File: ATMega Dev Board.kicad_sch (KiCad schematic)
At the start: 44 parts, among them J1 Conn_01x09, J2 Conn_01x04, J3 Conn_01x09, J4 SPI header, J5 USB-C_31-M-12, Q1 S8050, Q2 2N7002, Q3 HL6042, Q4 HL6042, SW1 SW_SPST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

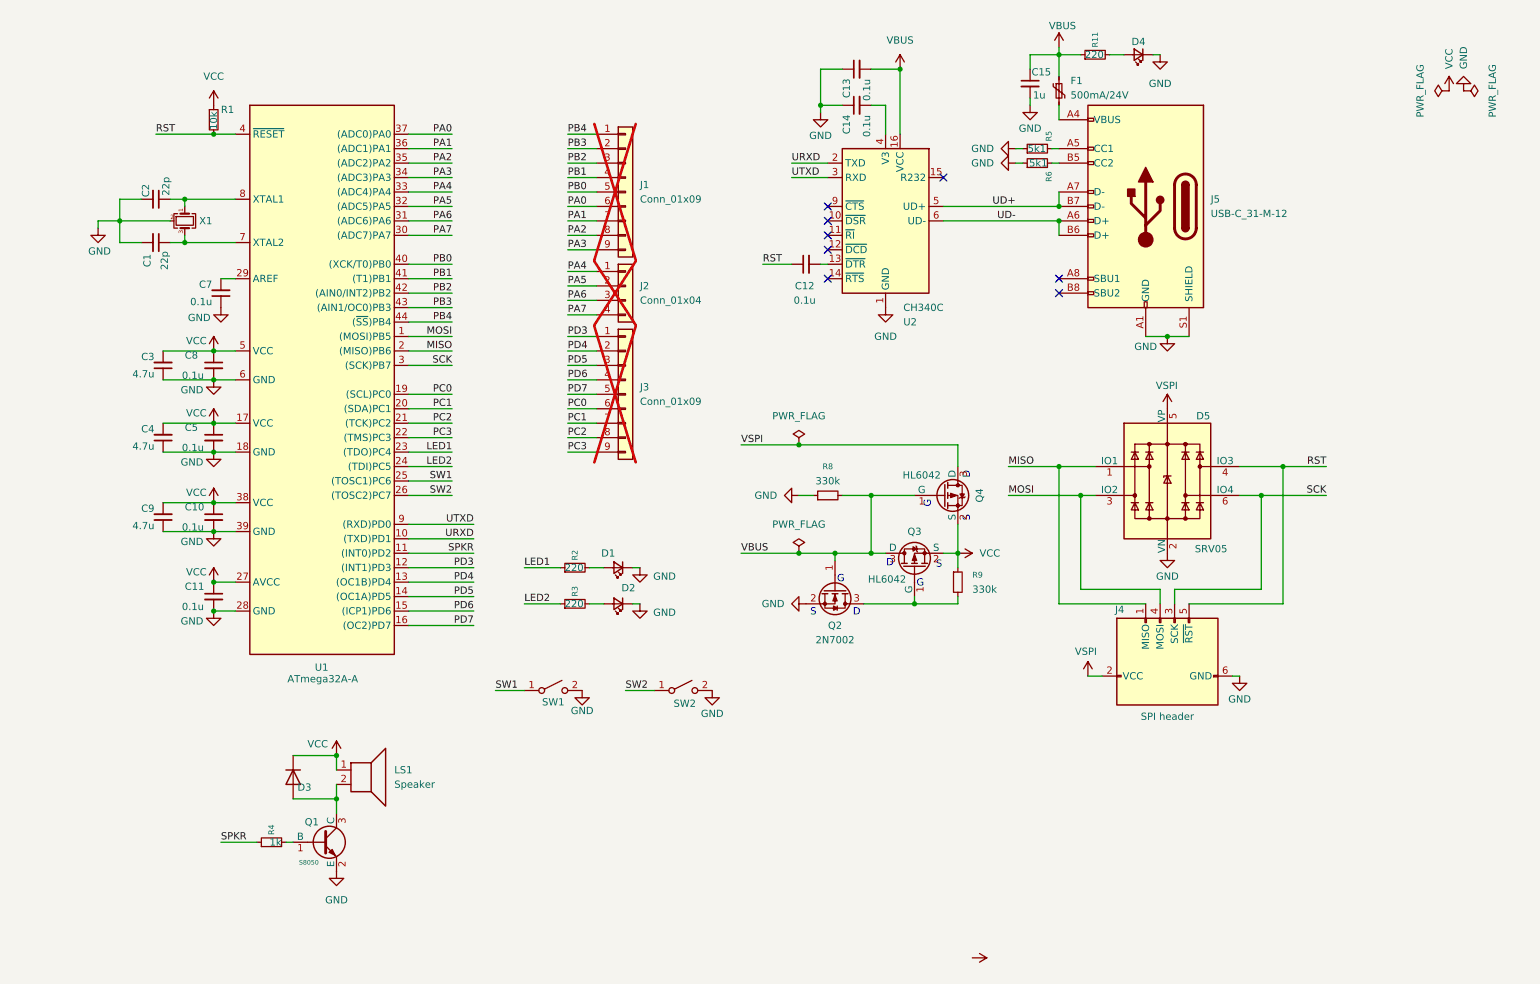
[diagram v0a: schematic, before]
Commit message: corrected usb connections
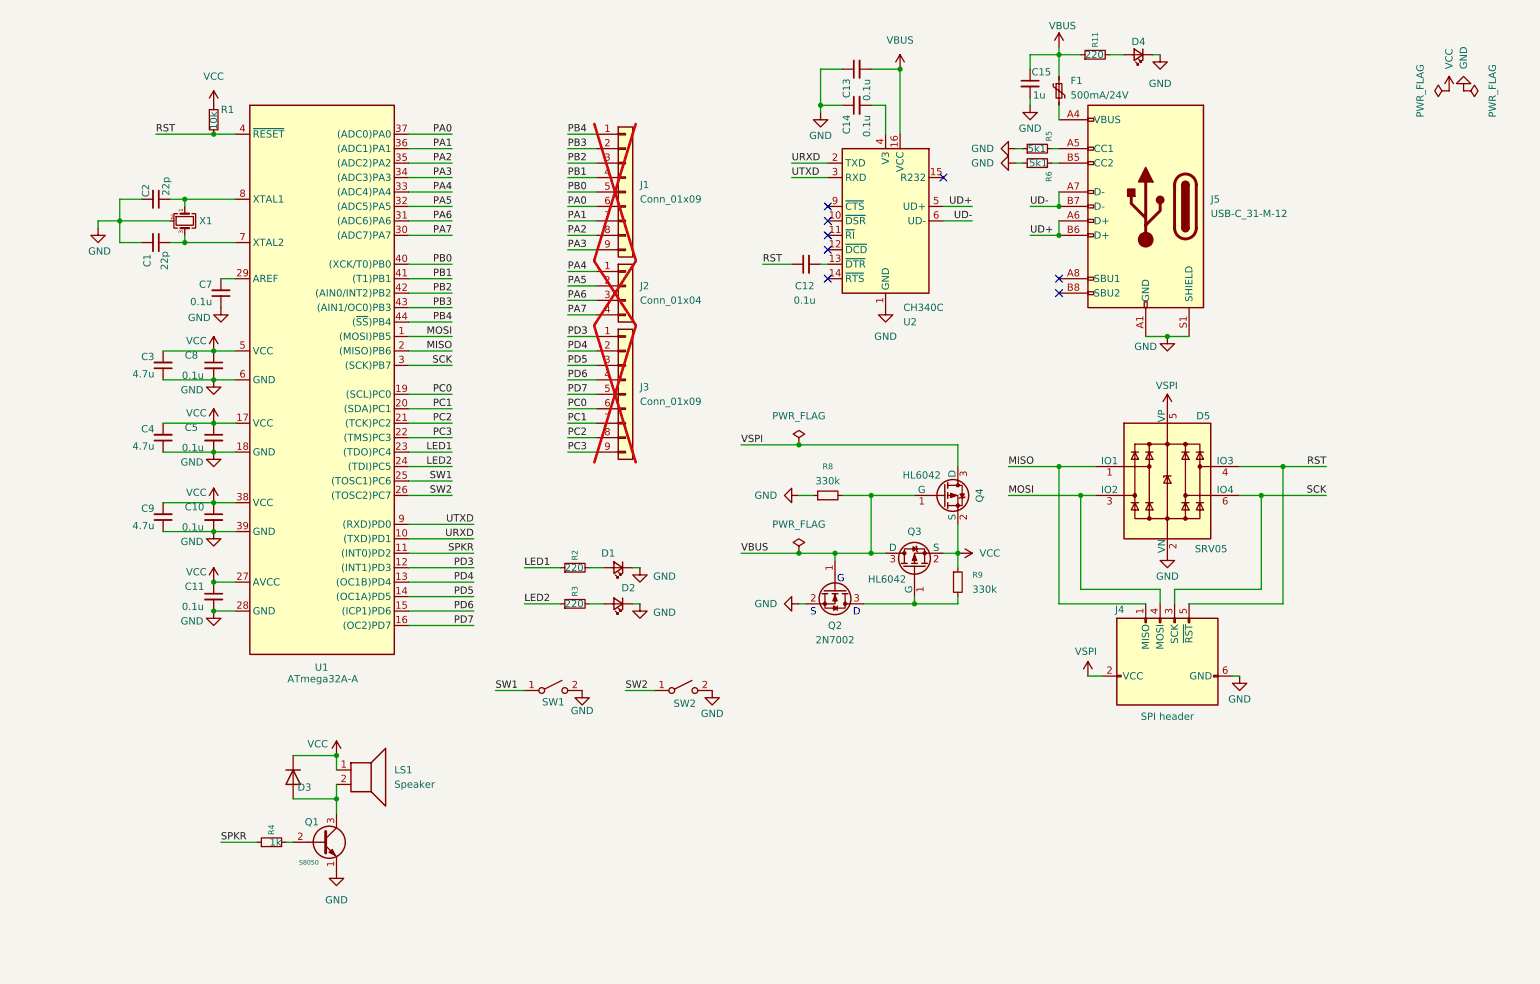
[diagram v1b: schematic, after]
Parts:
- Q1: footprint Package_TO_SOT_SMD:SOT-23-3 -> Package_TO_SOT_SMD:SOT-23; symbol PCM_JLCPCB-Transistors:NPN,S8050 -> Transistor_BJT:S8050
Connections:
- net GND: now also Q1.1 (E); no longer Q1.2 (E)
- net UD+: now also J5.A6 (D+), J5.B6 (D+); no longer J5.A7 (D-), J5.B7 (D-)
- net UD-: now also J5.A7 (D-), J5.B7 (D-); no longer J5.A6 (D+), J5.B6 (D+)
- net at R4.2: now also Q1.2 (B); no longer Q1.1 (B)
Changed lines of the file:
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@@
 	(text "G"
 		(exclude_from_sim no)
-		(at 175.006 115.824 0)
-		(effects
-			(font
-				(size 1.27 1.27)
-			)
-		)
-	)
-	(text "G"
-		(exclude_from_sim no)
 		(at 161.036 115.062 0)
 		(effects
@@
 	(text "S"
 		(exclude_from_sim no)
-		(at 178.308 112.522 0)
-		(effects
-			(font
-				(size 1.27 1.27)
-			)
-		)
-	)
-	(text "S"
-		(exclude_from_sim no)
-		(at 183.134 104.394 90)
-		(effects
-			(font
-				(size 1.27 1.27)
-			)
-		)
-	)
-	(text "S"
-		(exclude_from_sim no)
 		(at 156.21 120.904 0)
 		(effects
@@
 	(text "D"
 		(exclude_from_sim no)
-		(at 169.672 112.268 0)
-		(effects
-			(font
-				(size 1.27 1.27)
-			)
-		)
-	)
-	(text "D"
-		(exclude_from_sim no)
 		(at 163.83 120.904 0)
 		(effects
@@
 		)
 	)
-	(text "G"
-		(exclude_from_sim no)
-		(at 176.276 101.854 90)
-		(effects
-			(font
-				(size 1.27 1.27)
-			)
-		)
-	)
-	(text "D"
-		(exclude_from_sim no)
-		(at 183.134 96.774 90)
-		(effects
-			(font
-				(size 1.27 1.27)
-			)
-		)
-	)
 	(junction
 		(at 171.45 25.4)
@@
 	)
 	(junction
-		(at 199.39 49.53)
-		(diameter 0)
-		(color 0 0 0 0)
-	)
-	(junction
 		(at 72.39 146.05)
 		(diameter 0)
@@
 	)
 	(junction
+		(at 199.39 49.53)
+		(diameter 0)
+		(color 0 0 0 0)
+	)
+	(junction
 		(at 34.29 52.07)
 		(diameter 0)
@@
 	)
 	(junction
+		(at 199.39 54.61)
+		(diameter 0)
+		(color 0 0 0 0)
+	)
+	(junction
 		(at 234.95 100.33)
 		(diameter 0)
@@
 	)
 	(junction
-		(at 199.39 52.07)
-		(diameter 0)
-		(color 0 0 0 0)
-	)
-	(junction
 		(at 45.72 55.88)
 		(diameter 0)
@@
 	(wire
 		(pts
+			(xy 179.07 49.53) (xy 184.15 49.53)
+		)
+		(stroke
+			(width 0)
+			(type default)
+		)
+	)
+	(wire
+		(pts
 			(xy 85.09 36.83) (xy 92.71 36.83)
 		)
@@
 	(wire
 		(pts
-			(xy 179.07 49.53) (xy 199.39 49.53)
-		)
-		(stroke
-			(width 0)
-			(type default)
-		)
-	)
-	(wire
-		(pts
 			(xy 85.09 82.55) (xy 92.71 82.55)
 		)
@@
 	(wire
 		(pts
+			(xy 194.31 49.53) (xy 199.39 49.53)
+		)
+		(stroke
+			(width 0)
+			(type default)
+		)
+	)
+	(wire
+		(pts
 			(xy 153.67 100.33) (xy 156.21 100.33)
 		)
@@
 	(wire
 		(pts
+			(xy 194.31 54.61) (xy 199.39 54.61)
+		)
+		(stroke
+			(width 0)
+			(type default)
+		)
+	)
+	(wire
+		(pts
 			(xy 157.48 59.69) (xy 158.75 59.69)
 		)
@@
 	(wire
 		(pts
-			(xy 179.07 52.07) (xy 199.39 52.07)
+			(xy 50.8 101.6) (xy 54.61 101.6)
 		)
 		(stroke
@@
 	(wire
 		(pts
-			(xy 50.8 101.6) (xy 54.61 101.6)
+			(xy 234.95 116.84) (xy 234.95 100.33)
 		)
 		(stroke
@@
 	(wire
 		(pts
-			(xy 234.95 116.84) (xy 234.95 100.33)
+			(xy 63.5 161.29) (xy 64.77 161.29)
 		)
 		(stroke
@@
 	(wire
 		(pts
-			(xy 63.5 161.29) (xy 64.77 161.29)
+			(xy 41.91 101.6) (xy 50.8 101.6)
 		)
 		(stroke
@@
 	(wire
 		(pts
-			(xy 41.91 101.6) (xy 50.8 101.6)
+			(xy 113.03 44.45) (xy 118.11 44.45)
 		)
 		(stroke
@@
 	(wire
 		(pts
-			(xy 113.03 44.45) (xy 118.11 44.45)
+			(xy 50.8 120.65) (xy 54.61 120.65)
 		)
 		(stroke
@@
 	(wire
 		(pts
-			(xy 50.8 120.65) (xy 54.61 120.65)
+			(xy 123.19 134.62) (xy 128.27 134.62)
 		)
 		(stroke
@@
 	(wire
 		(pts
-			(xy 123.19 134.62) (xy 128.27 134.62)
+			(xy 153.67 119.38) (xy 154.94 119.38)
 		)
 		(stroke
@@
 	(wire
 		(pts
+			(xy 179.07 52.07) (xy 184.15 52.07)
+		)
+		(stroke
+			(width 0)
+			(type default)
+		)
+	)
+	(wire
+		(pts
 			(xy 85.09 41.91) (xy 92.71 41.91)
 		)
@@
 	)
 	(label "UD-"
-		(at 191.77 52.07 180)
+		(at 184.15 52.07 180)
 		(effects
 			(font
@@
 		)
 	)
+	(label "UD-"
+		(at 194.31 49.53 0)
+		(effects
+			(font
+				(size 1.27 1.27)
+			)
+			(justify left bottom)
+		)
+	)
 	(label "PA1"
 		(at 113.03 52.07 0)
@@
 		)
 	)
+	(label "UD+"
+		(at 194.31 54.61 0)
+		(effects
+			(font
+				(size 1.27 1.27)
+			)
+			(justify left bottom)
+		)
+	)
 	(label "PB2"
 		(at 92.71 64.77 180)
@@
 	)
 	(label "UD+"
-		(at 191.77 49.53 180)
+		(at 184.15 49.53 180)
 		(effects
 			(font
@@
 	(symbol
 		(lib_id "power:GND")
-		(at 154.94 119.38 270)
+		(at 153.67 119.38 270)
 		(unit 1)
 		(exclude_from_sim no)
@@
 		(fields_autoplaced yes)
 		(property "Reference" "#PWR0103"
-			(at 148.59 119.38 0)
+			(at 147.32 119.38 0)
 			(effects
 				(font
@@
 		)
 		(property "Value" "GND"
-			(at 151.13 119.3799 90)
+			(at 149.86 119.3799 90)
 			(effects
 				(font
@@
 		)
 		(property "Footprint" ""
-			(at 154.94 119.38 0)
+			(at 153.67 119.38 0)
 			(effects
 				(font
@@
 		)
 		(property "Datasheet" ""
-			(at 154.94 119.38 0)
+			(at 153.67 119.38 0)
 			(effects
 				(font
@@
 		)
 		(property "Description" "Power symbol creates a global label with name \"GND\" , ground"
-			(at 154.94 119.38 0)
+			(at 153.67 119.38 0)
 			(effects
 				(font
@@
 	)
 	(symbol
-		(lib_id "PCM_JLCPCB-Transistors:NPN,S8050")
+		(lib_id "Transistor_BJT:S8050")
 		(at 69.85 161.29 0)
 		(unit 1)
@@
 			)
 		)
-		(property "Footprint" "Package_TO_SOT_SMD:SOT-23-3"
-			(at 68.072 161.29 90)
+		(property "Footprint" "Package_TO_SOT_SMD:SOT-23"
+			(at 74.93 163.195 0)
 			(effects
 				(font
 					(size 1.27 1.27)
+					(italic yes)
 				)
+				(justify left)
 				(hide yes)
 			)
 		)
-		(property "Datasheet" ""
+		(property "Datasheet" "http://www.unisonic.com.tw/datasheet/S8050.pdf"
 			(at 69.85 161.29 0)
 			(effects
@@
 					(size 1.27 1.27)
 				)
+				(justify left)
 				(hide yes)
 			)
 		)
-		(property "Description" ""
+		(property "Description" "0.7A Ic, 20V Vce, Low Voltage High Current NPN Transistor, TO-92"
 			(at 69.85 161.29 0)
 			(effects
@@
 			)
 		)
+		(property "Sim.Device" "NPN"
+			(at 69.85 161.29 0)
+			(effects
+				(font
+					(size 1.27 1.27)
+				)
+				(hide yes)
+			)
+		)
+		(property "Sim.Pins" "1=E 2=B 3=C"
+			(at 69.85 161.29 0)
+			(effects
+				(font
+					(size 1.27 1.27)
+				)
+				(hide yes)
+			)
+		)
 		(pin "3"
 		)
@@
 					(unit 1)
 				)
-			)
-		)
-	)
-	(symbol
-		(lib_id "power:VCC")
-		(at 184.15 181.61 270)
-		(unit 1)
-		(exclude_from_sim no)
-		(in_bom yes)
-		(on_board yes)
-		(dnp no)
-		(property "Reference" "#PWR0101"
-			(at 180.34 181.61 0)
-			(effects
-				(font
-					(size 1.27 1.27)
-				)
-				(hide yes)
-			)
-		)
-		(property "Value" "VCC"
-			(at 184.15 168.148 90)
-			(effects
-				(font
-					(size 1.27 1.27)
-				)
-				(justify left)
-				(hide yes)
-			)
-		)
-		(property "Footprint" ""
-			(at 184.15 181.61 0)
-			(effects
-				(font
-					(size 1.27 1.27)
-				)
-				(hide yes)
-			)
-		)
-		(property "Datasheet" ""
-			(at 184.15 181.61 0)
-			(effects
-				(font
-					(size 1.27 1.27)
-				)
-				(hide yes)
-			)
-		)
-		(property "Description" "Power symbol creates a global label with name \"VCC\""
-			(at 184.15 181.61 0)
-			(effects
-				(font
-					(size 1.27 1.27)
-				)
-				(hide yes)
-			)
-		)
-		(pin "1"
-		)
-		(instances
-			(project "Power ORing"
-				(path "/6360eb7f-9406-4238-abc5-4989009a1856"
-					(reference "#PWR06")
-					(unit 1)
-				)
-			)
-			(project ""
-				(path "/70bbf962-aa97-42ae-8e7e-b12a946a1ea0"
-					(reference "#PWR0101")
-					(unit 1)
-				)

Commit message: added USB ESD protection
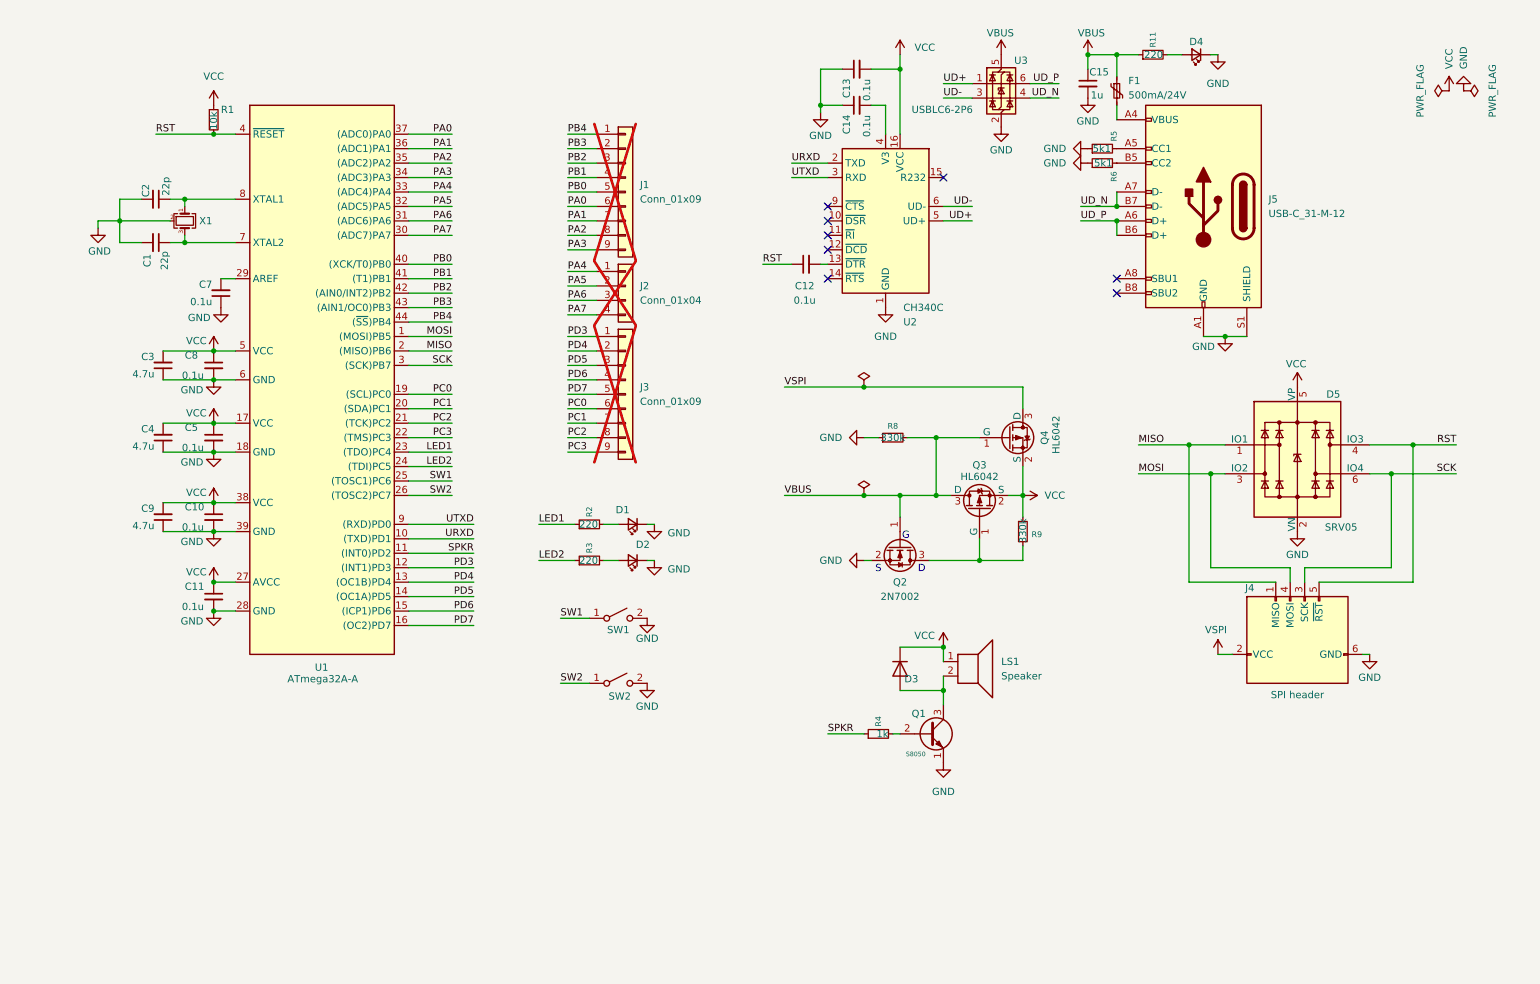
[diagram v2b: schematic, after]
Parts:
- added U3: USBLC6-2P6, Package_TO_SOT_SMD:SOT-666, symbol Power_Protection:USBLC6-2P6
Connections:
- net GND: now also U3.2 (GND)
- net UD+: now also U3.1 (I/O1); no longer J5.A6 (D+), J5.B6 (D+)
- net UD-: now also U3.3 (I/O2); no longer J5.A7 (D-), J5.B7 (D-)
- net VBUS: now also U3.5 (VBUS); no longer C13.2, U2.16 (VCC)
- net VCC: now also C13.2, D5.5 (VP), U2.16 (VCC)
- net VSPI: no longer D5.5 (VP)
- new net UD_N: J5.A7 (D-), J5.B7 (D-), U3.4 (I/O2)
- new net UD_P: J5.A6 (D+), J5.B6 (D+), U3.6 (I/O1)
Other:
- moved on the sheet: C15, D1, D2, D3, D4, D5, F1, J4, J5, LS1, Q1, Q2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

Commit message: correct UART signalling
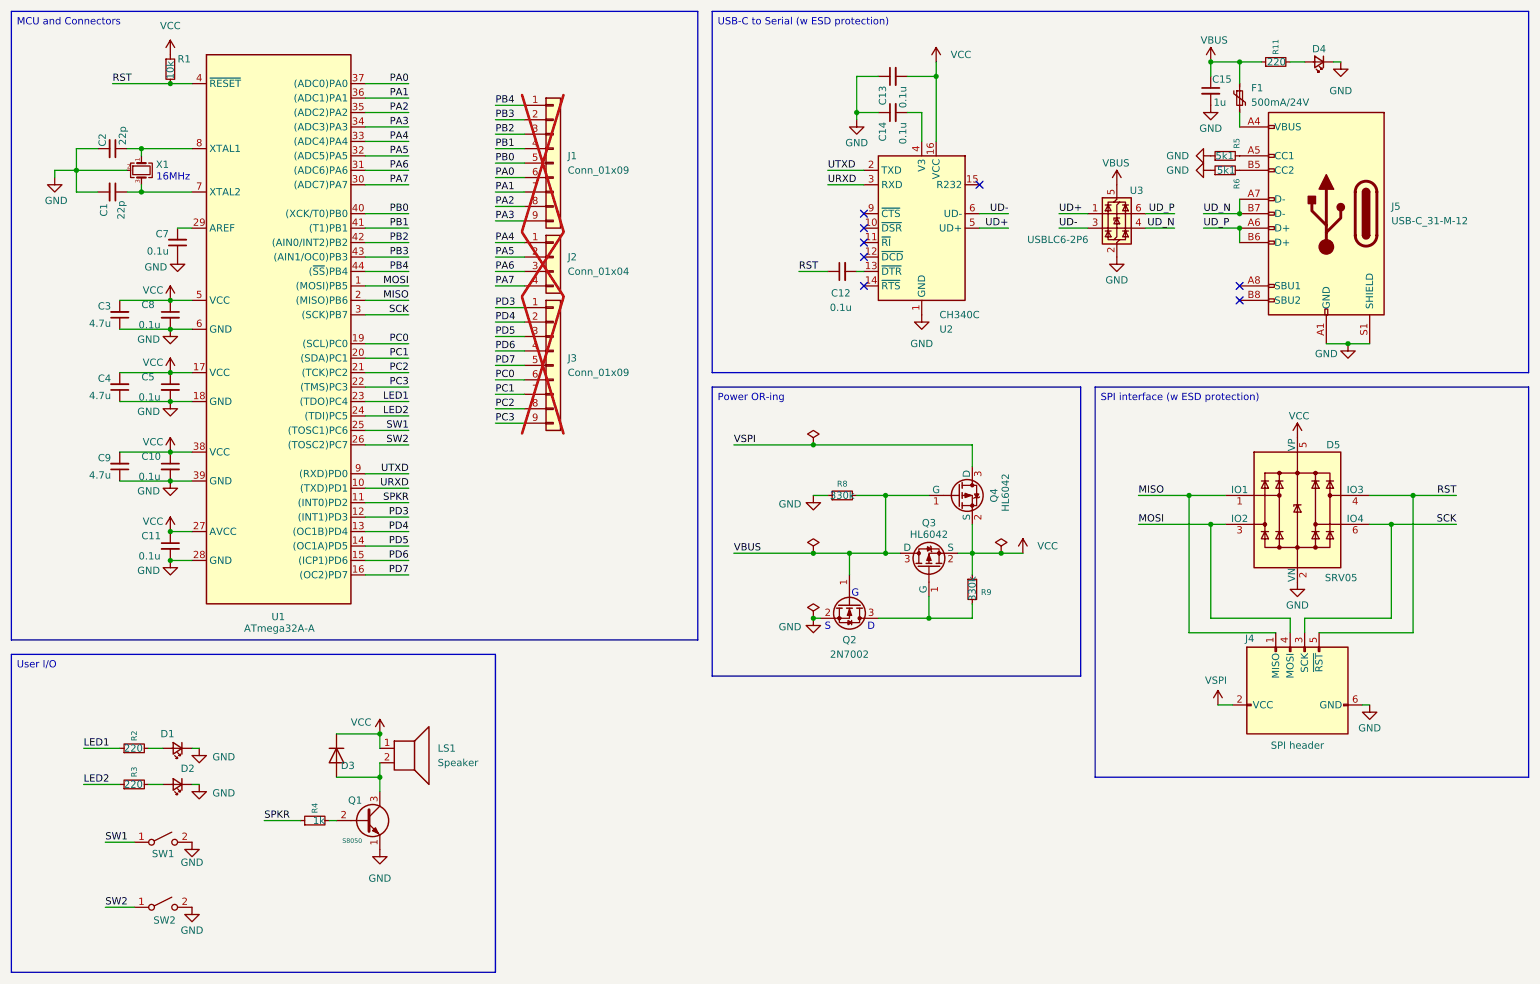
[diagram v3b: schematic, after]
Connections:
- net URXD: now also U2.3 (RXD); no longer U2.2 (TXD)
- net UTXD: now also U2.2 (TXD); no longer U2.3 (RXD)
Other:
- note added: "16MHz"
- title: (none) -> ATMega32 Test Board
- moved on the sheet: C1, C10, C11, C12, C13, C14, C15, C2, C3, C4, C5, C7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
